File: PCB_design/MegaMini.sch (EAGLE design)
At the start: 17 parts, among them IC1 ATMEGA2560-16AU, IC2 DS1307

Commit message: Finished the schematic
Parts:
- added C3, C4: 0.1µF, C_MC1206B104K500CT:MC1206B104K500CT
- added J1: AVR_SPI_PROG_3X2NS, SparkFun-Connectors:AVR_SPI_PROG_3X2NS
- added J2: (no value), SparkFun-Connectors:6_PIN_SERIAL_TARGET
- added J3: (no value), SparkFun-Connectors:CONN_02
- added J4: (no value), SparkFun-Connectors:CONN_25
- added R6: 10K, C_ERJ8ENF1002V:ERJ-8ENF1002V
- added RST_SWITCH: FSM4JRT, C_FSM4JRT:FSM4JRT
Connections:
- net 13 renamed PB7
- net SCL renamed PD0
- net SDA renamed PD1
- removed net DATAPIN_DHT11: IC1.PH5(OC4C)
- removed net DATAPIN_DS18B20_1: IC1.PH4(OC4B)
- removed net DATAPIN_DS18B20_2: IC1.PH3(OC4A)
- removed net DB4: IC1.(A14)PC6
- removed net DB5: IC1.(A13)PC5
- removed net DB6: IC1.(A12)PC4
- removed net DB7: IC1.(A11)PC3
- removed net EN: IC1.(A9)PC1
- removed net RS: IC1.(A10)PC2
- removed net SERVO_CONTROL: IC1.(OC1A/PCINT5)PB5
- removed net SQW: IC1.(OC3B/INT4)PE4, IC2.SQW/OUT, R5.2
- new net DTR: C3.1, J2.DTR
- new net MISO: IC1.(MISO/PCINT3)PB3, J1.1
- new net MOSI: IC1.(MOSI/PCINT2)PB2, J1.4
- new net PB4: IC1.(OC2A/PCINT4)PB4, J4.8
- new net PB5: IC1.(OC1A/PCINT5)PB5, J4.9
- new net PB6: IC1.(OC1B/PCINT6)PB6, J4.10
- new net PE3: IC1.(OC3A/AIN1)PE3, J4.11
- new net PE4: IC1.(OC3B/INT4)PE4, IC2.SQW/OUT, J4.12, R5.2
- new net PE5: IC1.(OC3C/INT5)PE5, J4.13
- new net PG5: IC1.(OC0B)PG5, J4.14
- new net PH3: IC1.PH3(OC4A), J4.15
- new net PH4: IC1.PH4(OC4B), J4.16
- new net PH5: IC1.PH5(OC4C), J4.17
- new net PH6: IC1.PH6(OC2B), J4.18
- new net PL3: IC1.PL3(OC5A), J4.19
- new net PL4: IC1.PL4(OC5B), J4.20
- new net PL5: IC1.PL5(OC5C), J4.21
- new net RX0: IC1.(RXD0/PCIN8)PE0, J2.RXI
- new net SCK: IC1.(SCK/PCINT1)PB1, J1.3
- new net TX0: IC1.(TXD0)PE1, J2.TXO
- net AREF: now also C4.2
- net GND: now also C4.1, J1.6, J2.CTS, J2.GND, J3.2, J4.4, J4.5, J4.6, J4.7, RST_SWITCH.2
- net RST: now also C3.2, J1.5, R6.1, RST_SWITCH.1
- net VCC: now also J1.2, J2.VCC, J3.1, J4.22, J4.23, J4.24, J4.25, R6.2
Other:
- moved on the sheet: BATTERY, BC1, BC2, BC3, C1, C2, CRYSTAL1, CRYSTAL2, IC2, LED1, LED2, R1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

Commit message: revision 1.0 pcb design
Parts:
- removed BATTERY: 1066, C_1066:1066
- removed CRYSTAL2: 32.768KHz, C_Q13FC13500004_FC-135_32.768KHZ:Q13FC13500004_FC-135_32.768KHZ
- removed R5: 10K, C_ERJ8ENF1002V:ERJ-8ENF1002V
- added BT1: Keystone 3001, SparkFun-Batteries:BATTERY-12MM_PTH
- added XTAL2: 32.768KHz, C_Q13FC13500004_FC-135_32.768KHZ:Q13FC13500004_FC-135_32.768KHZ
- IC1: value ATMEGA2560-16AU -> 2560-16AU
- J4: device SparkFun-Connectors:CONN_25 -> SparkFun-Connectors:CONN_19
- renumbered CRYSTAL1 to XTAL1, RST_SWITCH to RST
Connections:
- removed net PL3: IC1.PL3(OC5A), J4.19
- removed net PL4: IC1.PL4(OC5B), J4.20
- removed net PL5: IC1.PL5(OC5C), J4.21
- new net SQW/OUT: IC2.SQW/OUT
- net GND: now also BT1.-, J4.12, J4.13, J4.14, J4.15; no longer BATTERY.-, J4.4, J4.5, J4.6, J4.7
- net N$3: now also XTAL2.1; no longer CRYSTAL2.1
- net N$4: now also XTAL2.2; no longer CRYSTAL2.2
- net N$5: now also BT1.+; no longer BATTERY.+
- net PB4: now also J4.3; no longer J4.8
- net PB5: now also J4.2; no longer J4.9
- net PB6: now also J4.1; no longer J4.10
- net PE3: now also J4.10; no longer J4.11
- net PE4: now also J4.9; no longer IC2.SQW/OUT, J4.12, R5.2
- net PE5: now also J4.8; no longer J4.13
- net PG5: now also J4.11; no longer J4.14
- net PH3: now also J4.7; no longer J4.15
- net PH4: now also J4.6; no longer J4.16
- net PH5: now also J4.5; no longer J4.17
- net PH6: now also J4.4; no longer J4.18
- net VCC: now also J4.16, J4.17, J4.18, J4.19; no longer J4.22, J4.23, J4.24, J4.25, R5.1
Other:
- moved on the sheet: IC2, J2, J3, R3, R4

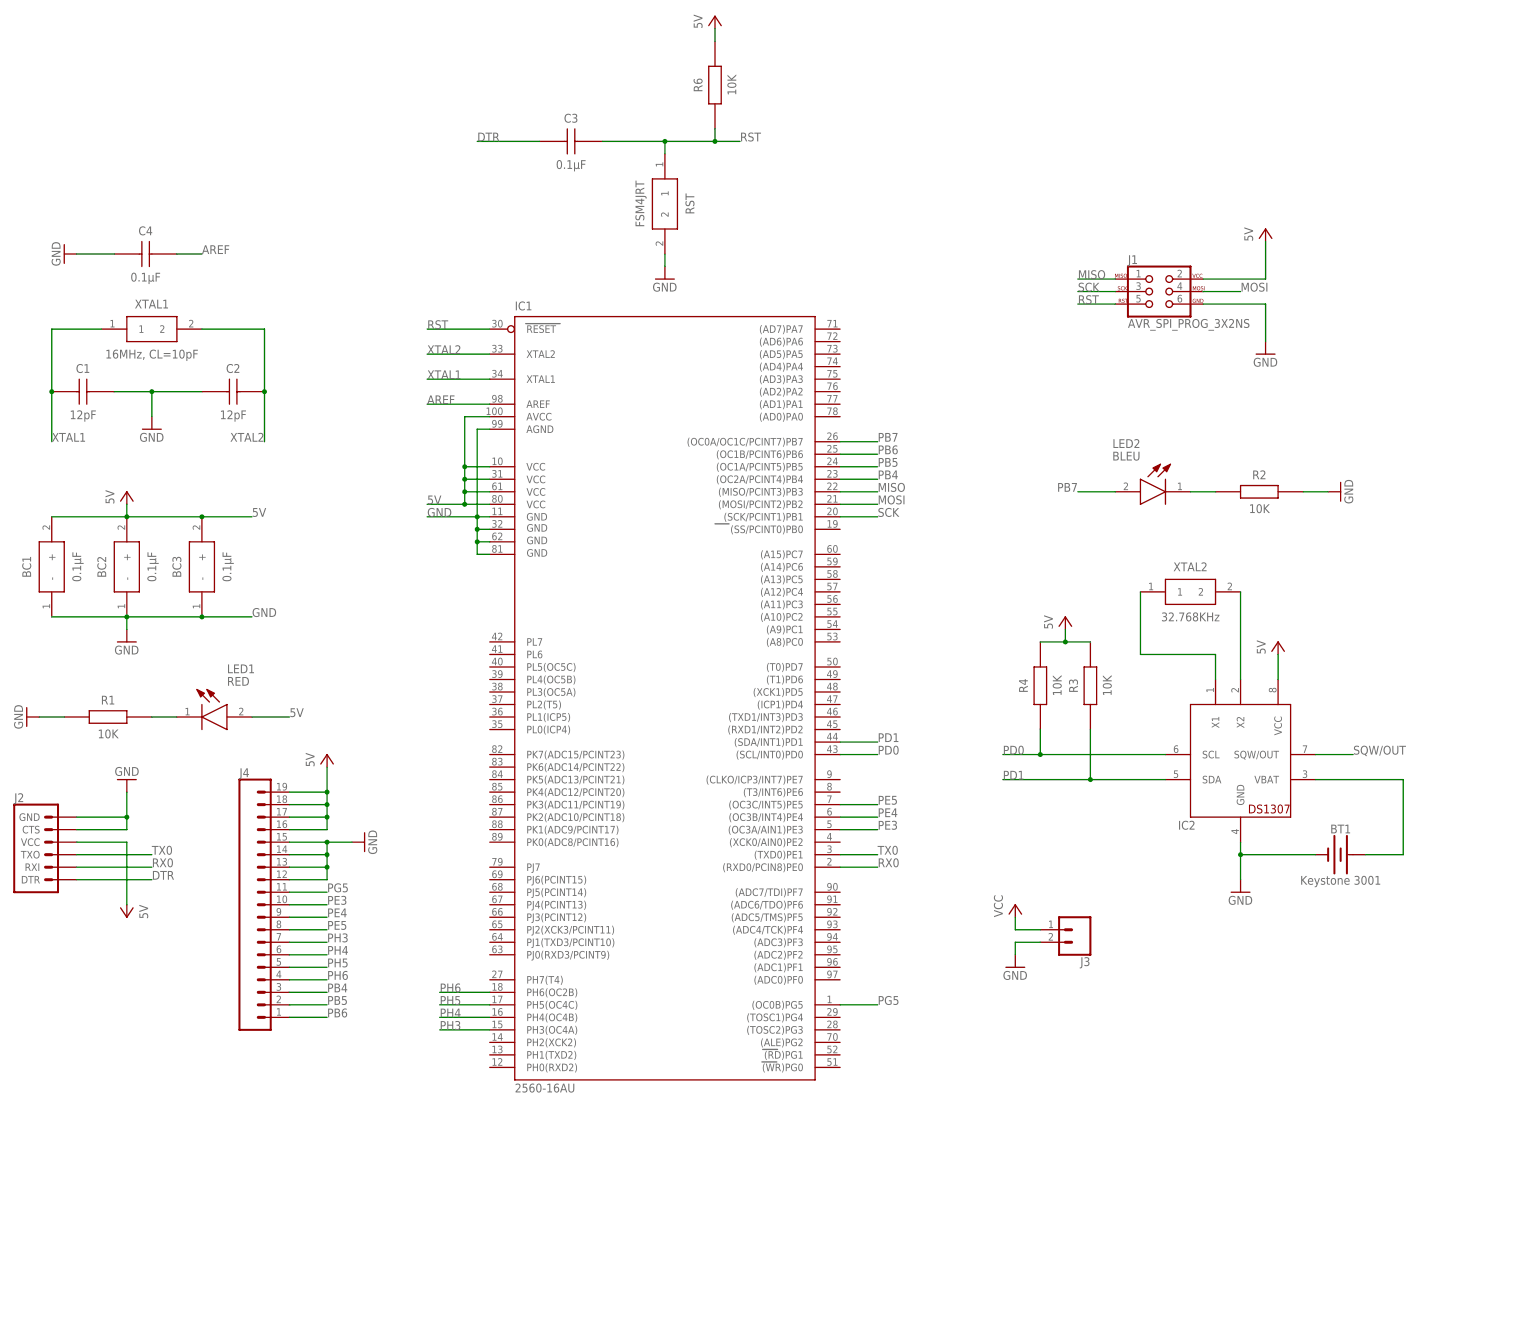
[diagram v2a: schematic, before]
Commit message: Finished revision 1.0 PCB and some major changes to the schematic
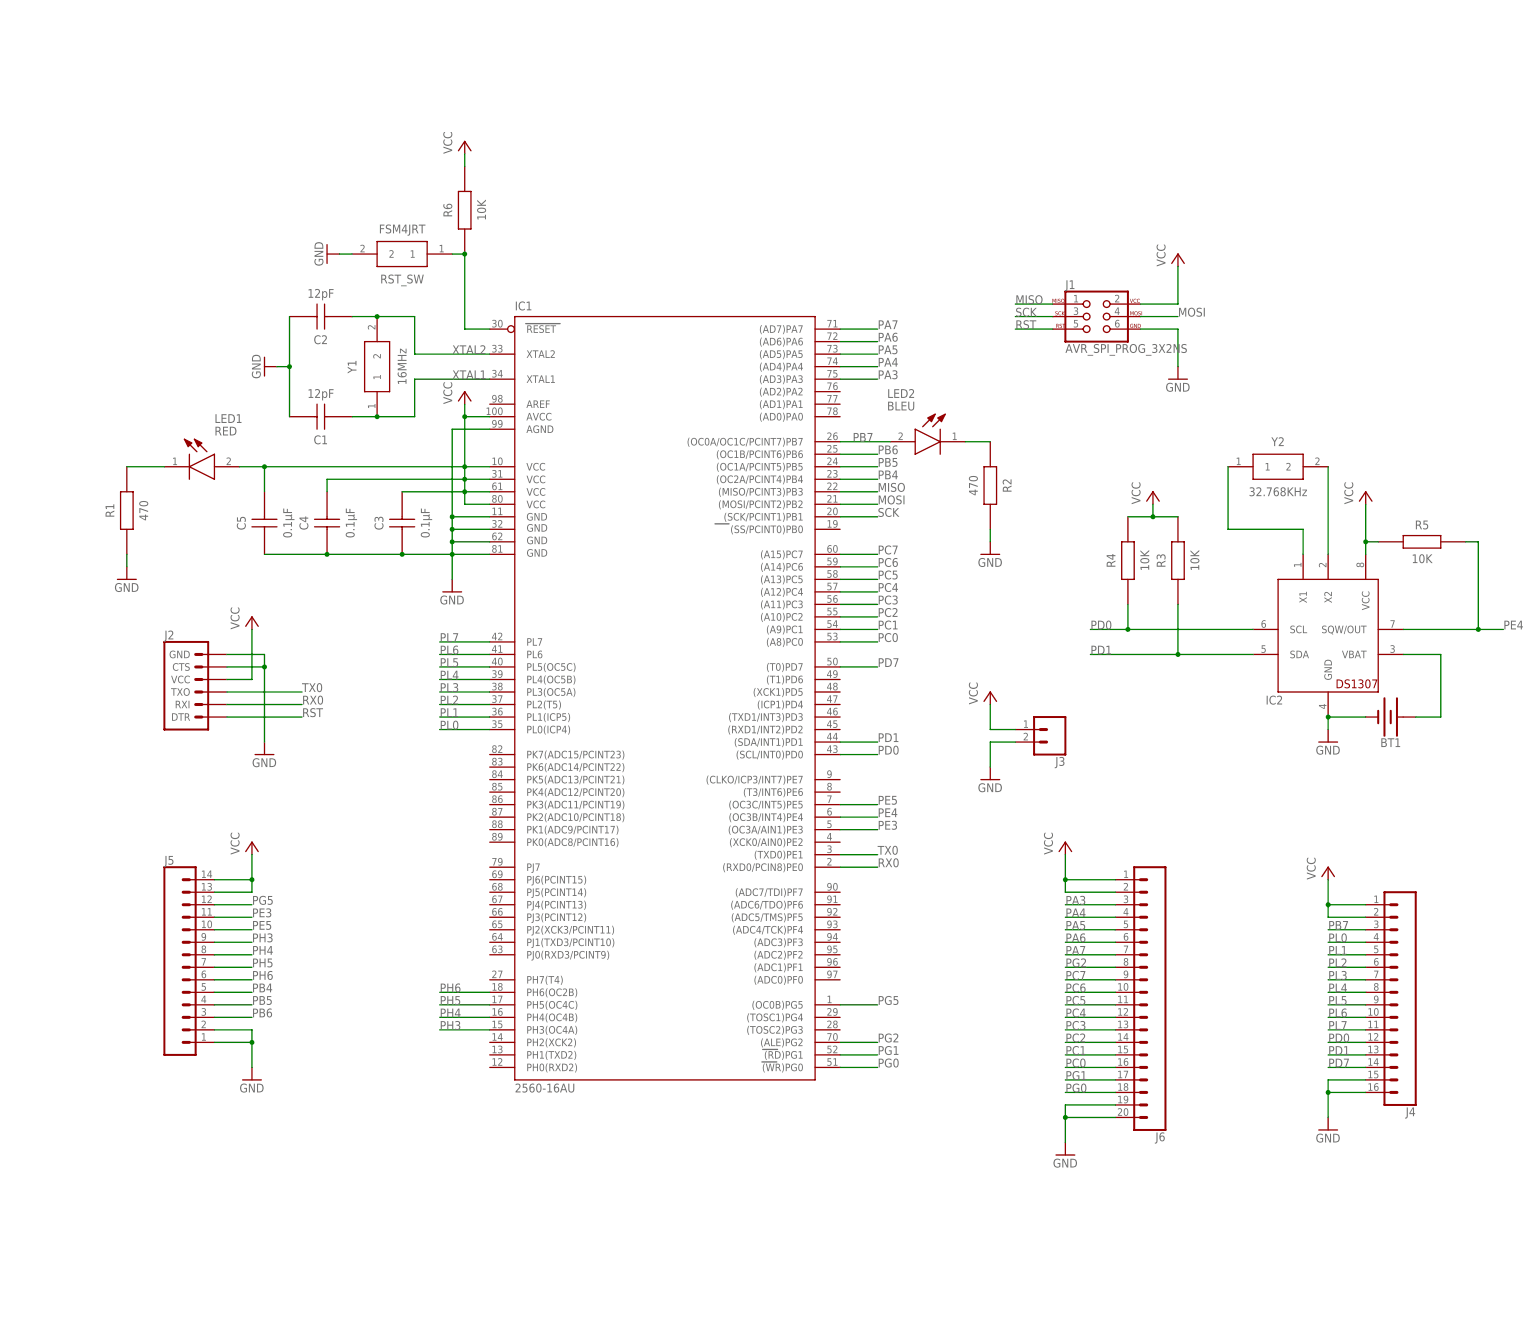
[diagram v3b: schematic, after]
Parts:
- removed BC1, BC2, BC3: 0.1µF, C_WCAP-AS5H Series:865230640001
- removed RST: FSM4JRT, C_FSM4JRT:FSM4JRT
- removed XTAL1: 16MHz, CL=10pF, C_FOXSDLF_160-20:FOXSDLF_160-20
- removed XTAL2: 32.768KHz, C_Q13FC13500004_FC-135_32.768KHZ:Q13FC13500004_FC-135_32.768KHZ
- added C5: 0.1µF, C_C1206C104K5RACTU:C1206C104K5RACTU
- added J5: (no value), SparkFun-Connectors:CONN_14
- added J6: (no value), SparkFun-Connectors:CONN_20
- added R5: 10K, C_ERJ8ENF1002V:ERJ-8ENF1002V
- added RST_SW: FSM4JRT, C_FSM4JRT:FSM4JRT
- added Y1: 16MHz, C_FOXSDLF_160-20:FOXSDLF_160-20
- added Y2: 32.768KHz, C_Q13FC13500004_FC-135_32.768KHZ:Q13FC13500004_FC-135_32.768KHZ
- BT1: value Keystone 3001 -> (none)
- C3, C4: device C_MC1206B104K500CT:MC1206B104K500CT -> C_C1206C104K5RACTU:C1206C104K5RACTU
- J4: device SparkFun-Connectors:CONN_19 -> SparkFun-Connectors:CONN_16
- R1, R2: value 10K -> 470; device C_ERJ8ENF1002V:ERJ-8ENF1002V -> C_ERJ8ENF4700V:ERJ8ENF4700V
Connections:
- removed net 5V: BC1.+, BC2.+, BC3.+, IC1.AVCC, IC1.VCC, IC1.VCC1, IC1.VCC2, IC1.VCC3, LED1.A
- removed net AREF: C4.2, IC1.AREF
- removed net DTR: C3.1, J2.DTR
- removed net N$2: LED2.K, R2.2
- removed net SQW/OUT: IC2.SQW/OUT
- new net N$1: IC1.RESET, R6.1, RST_SW.1
- new net N$15: LED2.K, R2.1
- new net PA3: IC1.(AD3)PA3, J6.3
- new net PA4: IC1.(AD4)PA4, J6.4
- new net PA5: IC1.(AD5)PA5, J6.5
- new net PA6: IC1.(AD6)PA6, J6.6
- new net PA7: IC1.(AD7)PA7, J6.7
- new net PC0: IC1.(A8)PC0, J6.16
- new net PC1: IC1.(A9)PC1, J6.15
- new net PC2: IC1.(A10)PC2, J6.14
- new net PC3: IC1.(A11)PC3, J6.13
- new net PC4: IC1.(A12)PC4, J6.12
- new net PC5: IC1.(A13)PC5, J6.11
- new net PC6: IC1.(A14)PC6, J6.10
- new net PC7: IC1.(A15)PC7, J6.9
- new net PD7: IC1.(T0)PD7, J4.14
- new net PG0: IC1.(WR)PG0, J6.18
- new net PG1: IC1.(RD)PG1, J6.17
- new net PG2: IC1.(ALE)PG2, J6.8
- new net PL0: IC1.PL0(ICP4), J4.4
- new net PL1: IC1.PL1(ICP5), J4.5
- new net PL2: IC1.PL2(T5), J4.6
- new net PL3: IC1.PL3(OC5A), J4.7
- new net PL4: IC1.PL4(OC5B), J4.8
- new net PL5: IC1.PL5(OC5C), J4.9
- new net PL6: IC1.PL6, J4.10
- new net PL7: IC1.PL7, J4.11
- net GND: now also C2.2, C3.1, C5.1, J4.16, J5.1, J5.2, J6.19, J6.20, R2.2, RST_SW.2; no longer BC1.-, BC2.-, BC3.-, C2.1, J4.12, J4.13, J4.14, R2.1, RST.2
- net N$3: now also Y2.1; no longer XTAL2.1
- net N$4: now also Y2.2; no longer XTAL2.2
- net PB4: now also J5.5; no longer J4.3
- net PB5: now also J5.4; no longer J4.2
- net PB6: now also J5.3; no longer J4.1
- net PB7: now also J4.3
- net PD0: now also J4.12
- net PD1: now also J4.13
- net PE3: now also J5.11; no longer J4.10
- net PE4: now also IC2.SQW/OUT, R5.2; no longer J4.9
- net PE5: now also J5.10; no longer J4.8
- net PG5: now also J5.12; no longer J4.11
- net PH3: now also J5.9; no longer J4.7
- net PH4: now also J5.8; no longer J4.6
- net PH5: now also J5.7; no longer J4.5
- net PH6: now also J5.6; no longer J4.4
- net RST: now also J2.DTR; no longer C3.2, IC1.RESET, R6.1, RST.1
- net VCC: now also C3.2, C4.2, C5.2, IC1.AVCC, IC1.VCC, IC1.VCC1, IC1.VCC2, IC1.VCC3, J4.1, J4.2, J5.13, J5.14, J6.1, J6.2, LED1.A, R5.1; no longer J4.16, J4.17, J4.18, J4.19
- net XTAL1: now also Y1.1; no longer XTAL1.1
- net XTAL2: now also C2.1, Y1.2; no longer C2.2, XTAL1.2
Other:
- moved on the sheet: BT1, C1, C2, C3, C4, IC2, J1, J2, J3, LED1, LED2, R1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

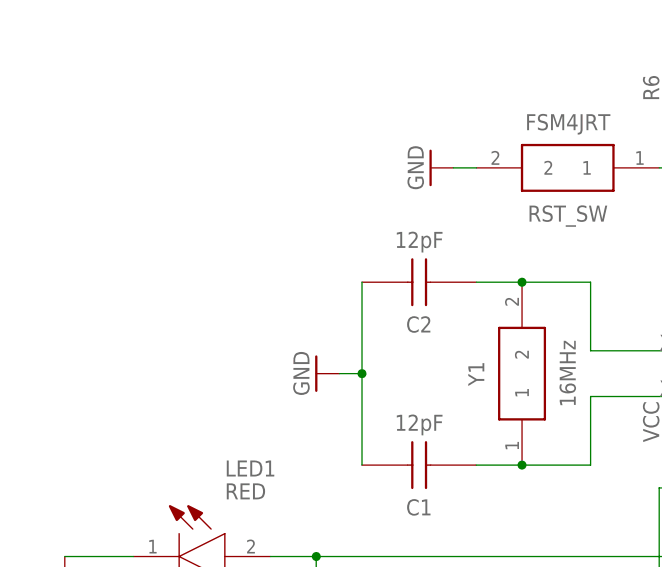
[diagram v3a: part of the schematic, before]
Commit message: Adjustements on the Atmel2560 package
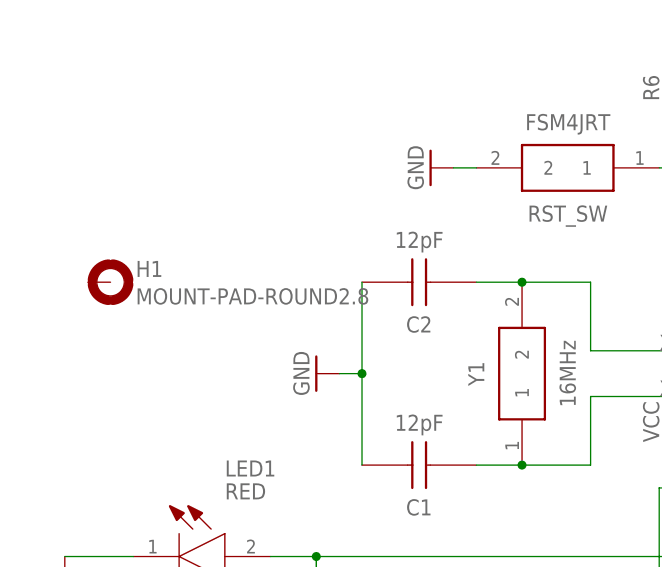
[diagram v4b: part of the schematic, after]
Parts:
- added H1: MOUNT-PAD-ROUND2.8, holes:MOUNT-PAD-ROUND2.8
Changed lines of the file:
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@@
 <part name="P+10" library="supply1" library_urn="urn:adsk.eagle:library:371" deviceset="VCC" device=""/>
 <part name="GND12" library="supply1" library_urn="urn:adsk.eagle:library:371" deviceset="GND" device=""/>
+<part name="H1" library="holes" library_urn="urn:adsk.eagle:library:237" deviceset="MOUNT-PAD-ROUND" device="2.8" package3d_urn="urn:adsk.eagle:package:14281/1"/>
 </parts>
 <sheets>
@@
 <instance part="P+10" gate="VCC" x="370.84" y="363.22"/>
 <instance part="GND12" gate="1" x="302.26" y="325.12"/>
+<instance part="H1" gate="G$1" x="307.34" y="378.46"/>
 </instances>
 <busses>
@@
 will not be understood (or retained) with this version.
 </note>
+<note version="8.3" severity="warning">
+Since Version 8.3, EAGLE supports the association of 3D packages
+with devices in libraries, schematics, and board files. Those 3D
+packages will not be understood (or retained) with this version.
+</note>
 </compatibility>
